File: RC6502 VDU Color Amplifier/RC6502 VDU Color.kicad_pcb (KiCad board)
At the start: 2 copper layers, 90.2 x 46.4 mm, 22 parts, among them J1 Video_IN, J2 Video_OUT, J3 VIDEO, J4 OSC_EN, Q1 2N3906, Q2 2N3904, U1 MC1372, Y1 3.579545

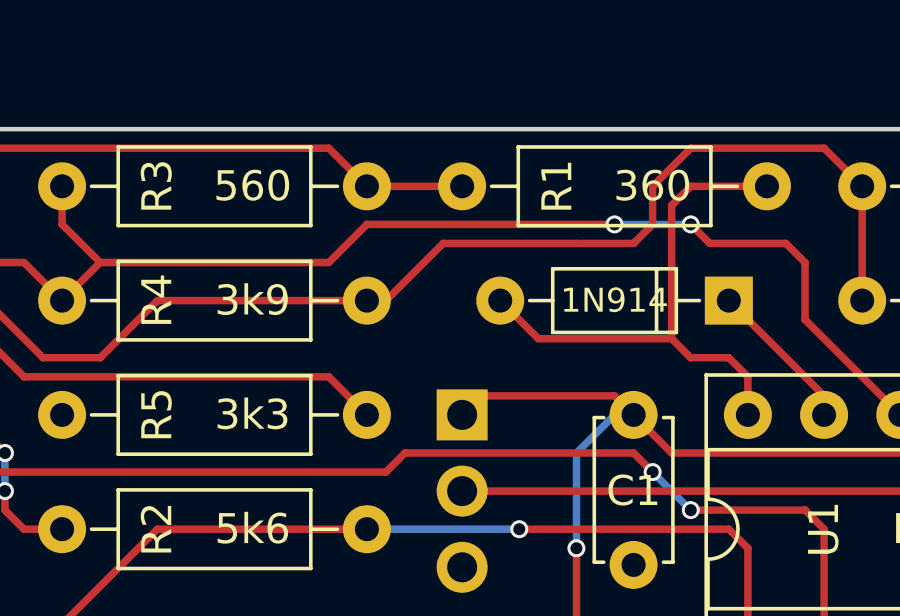
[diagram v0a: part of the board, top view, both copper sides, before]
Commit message: Forgot to actually power amplifier circuit :-(
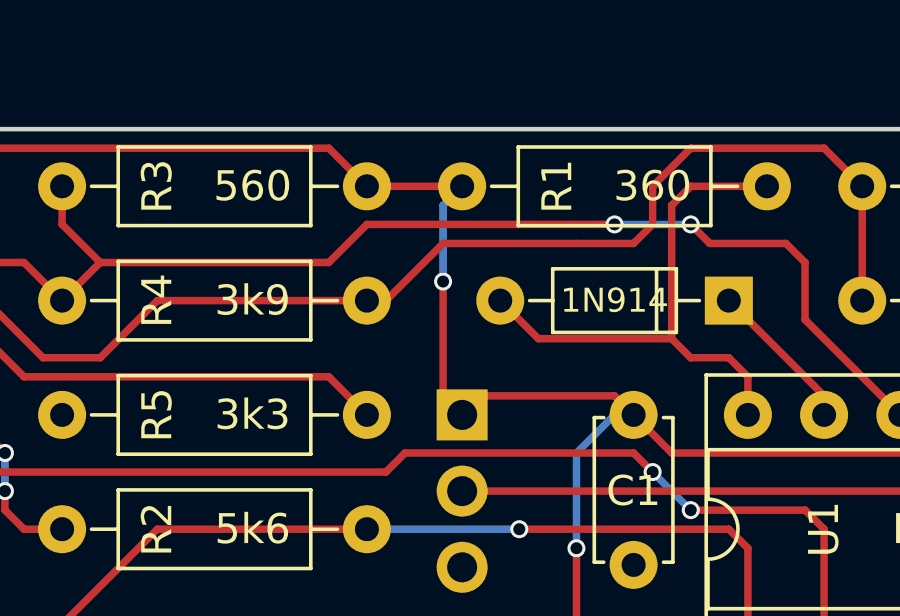
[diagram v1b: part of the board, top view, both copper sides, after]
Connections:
- Q1 pad 1: Net-(Q1-Pad1) -> VCC
- Q2 pad 3: Net-(Q1-Pad1) -> VCC
- R1 pad 1: Net-(Q1-Pad1) -> VCC
- R3 pad 1: Net-(Q1-Pad1) -> VCC
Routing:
- net VCC: track 29.8 -> 62.5 mm, vias 1 -> 2
- net Net-(Q1-Pad1): track 24.5 -> 0.00 mm
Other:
- board text added: "Revision B"
- board text removed: "Revision A"
